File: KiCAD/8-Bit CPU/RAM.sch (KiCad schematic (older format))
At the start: 10 parts, among them U4 74HC1G32, U5 6264SL

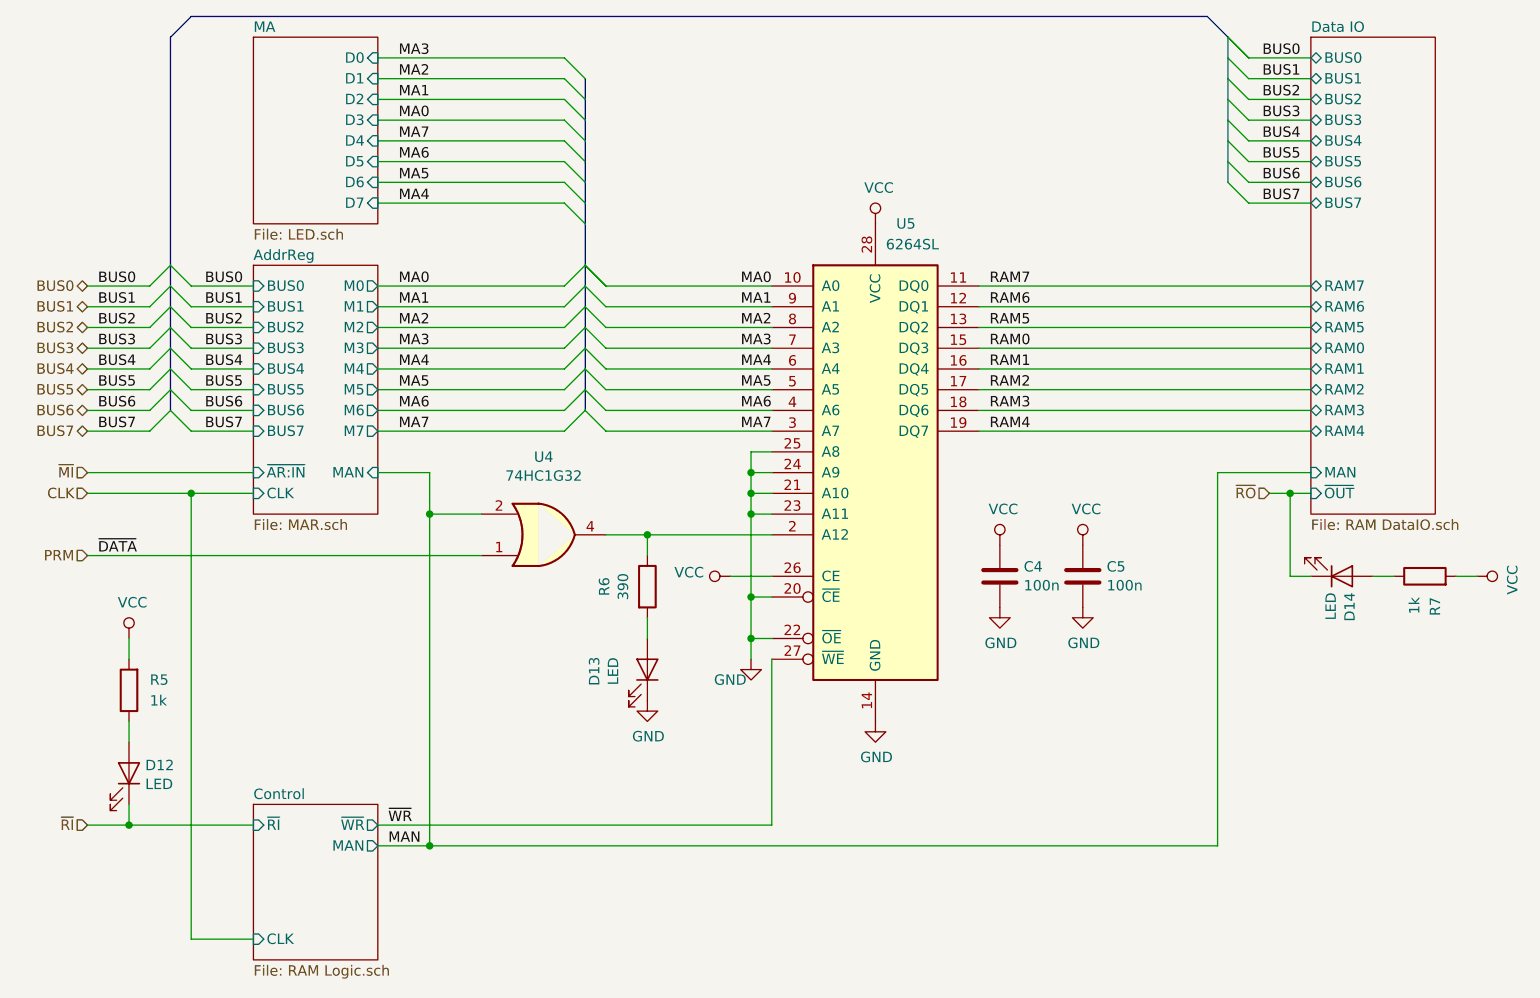
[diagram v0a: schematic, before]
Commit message: KiCAD cleanup - Revision A
Revision A Known Issues:
 * ATTiny45 has incorrect footprint
 * Flags register is redundant (The ATMega16's output port is a register)
 * Power jack pinout is wrong (12V shorted to ground)
 * Step counter reset logic is wrong (Active high signalling, Active low input)
 * ALU output indicator not connected
 * HLT indicator missing
 * EEPROMs can't be page written due to addressing setup (minor annoyance)
 * Flags Logic uses NAND gates instead of AND (fixed on the board I built)
 * Programmer needs to be able to toggle EEPROM outputs and Addressing Devices
    with different signals to enable reading.
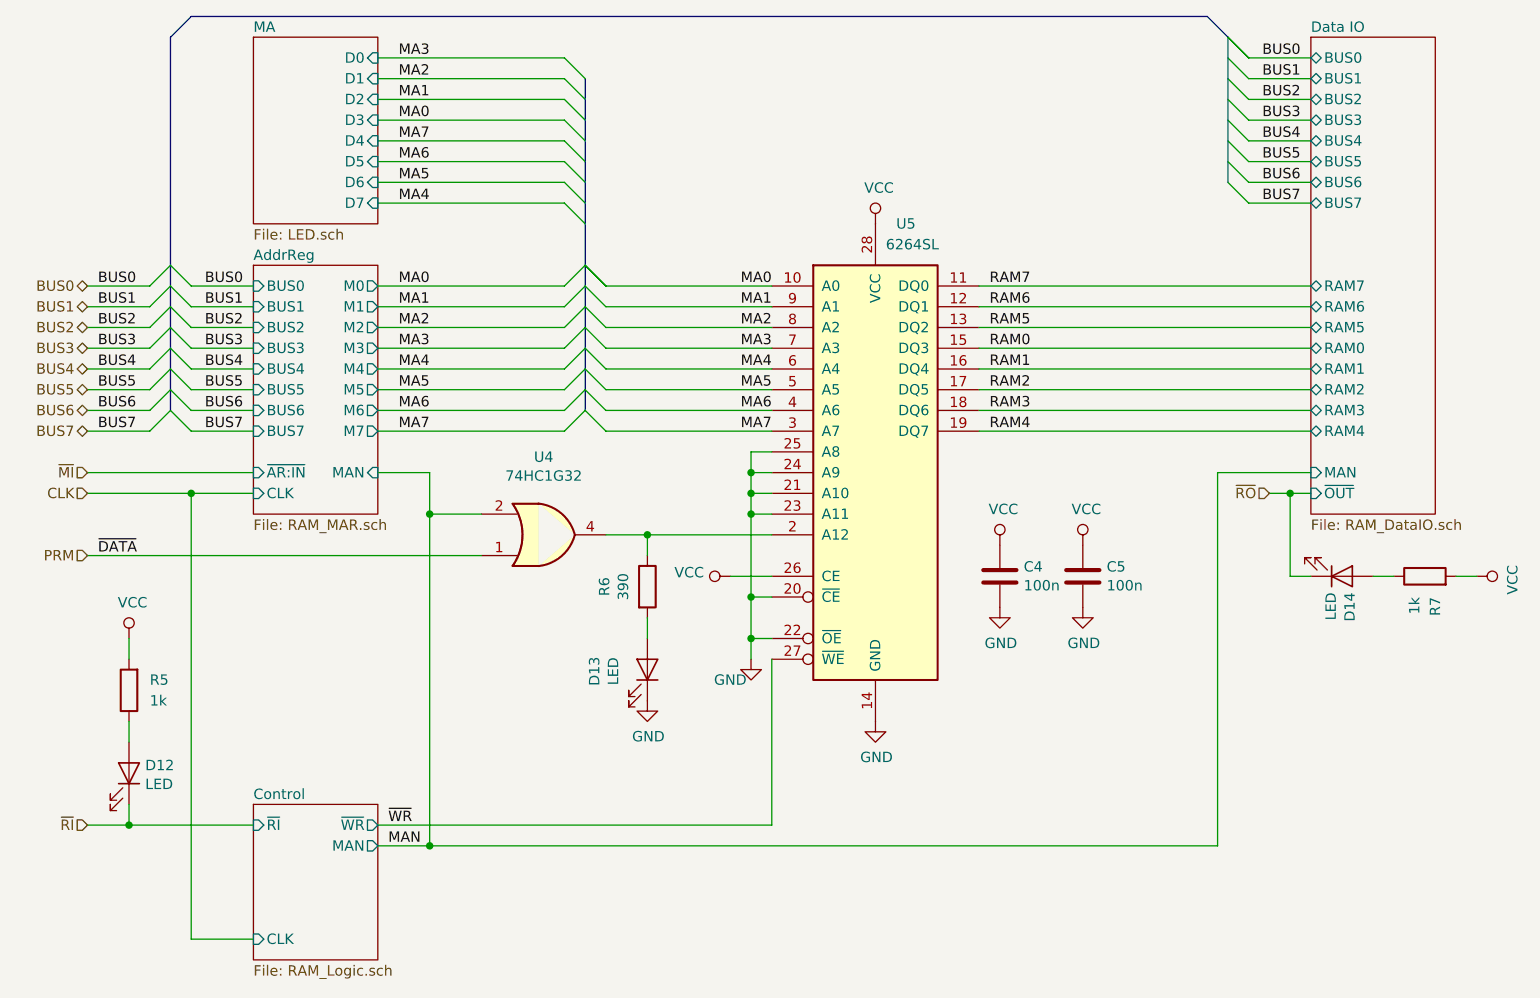
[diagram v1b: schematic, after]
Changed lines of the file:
@@
 $Descr A4 11693 8268
 encoding utf-8
-Sheet 4 30
+Sheet 4 29
 Title ""
 Date ""
@@
 U 5D5738D6
 F0 "AddrReg" 50
-F1 "MAR.sch" 50
+F1 "RAM_MAR.sch" 50
 F2 "M0" O R 3800 2600 50
 F3 "M2" O R 3800 2800 50
@@
 U 5D450B31
 F0 "Data IO" 50
-F1 "RAM DataIO.sch" 50
+F1 "RAM_DataIO.sch" 50
 F2 "RAM0" B L 8300 2900 50
 F3 "RAM1" B L 8300 3000 50
@@
 U 5D4645A0
 F0 "Control" 50
-F1 "RAM Logic.sch" 50
+F1 "RAM_Logic.sch" 50
 F2 "~RI" I L 3200 5200 50
 F3 "MAN" O R 3800 5300 50

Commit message: KiCAD files update & Gerbers
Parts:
- renumbered D14 to D12, D12 to D14, R7 to R5, R5 to R7, U5 to U4, U4 to U5
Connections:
- net GND: no longer D13.1 (K)
- net VCC: now also D13.2 (A)
- net at R6.2: now also D13.1 (K); no longer D13.2 (A)
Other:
- moved on the sheet: D13
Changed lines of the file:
@@
 Title ""
 Date ""
-Rev ""
+Rev "C"
 Comp ""
 Comment1 ""
@@
 $EndDescr
 $Comp
-L power:GND #PWR023
+L power:GND #PWR028
 U 1 1 5D6B09A3
 P 5600 4400
-F 0 "#PWR023" H 5600 4150 50  0001 C CNN
+F 0 "#PWR028" H 5600 4150 50  0001 C CNN
 F 1 "GND" H 5500 4300 50  0000 C CNN
 F 2 "" H 5600 4400 50  0001 C CNN
@@
 	5600 3700 5600 3600
 $Comp
-L power:GND #PWR025
+L power:GND #PWR029
 U 1 1 5D6B12D2
 P 6200 4700
-F 0 "#PWR025" H 6200 4450 50  0001 C CNN
+F 0 "#PWR029" H 6200 4450 50  0001 C CNN
 F 1 "GND" H 6205 4527 50  0000 C CNN
 F 2 "" H 6200 4700 50  0001 C CNN
@@
 $EndComp
 $Comp
-L power:VCC #PWR024
+L power:VCC #PWR020
 U 1 1 5D6B14C7
 P 6200 2300
-F 0 "#PWR024" H 6200 2150 50  0001 C CNN
+F 0 "#PWR020" H 6200 2150 50  0001 C CNN
 F 1 "VCC" H 6217 2473 50  0000 C CNN
 F 2 "" H 6200 2300 50  0001 C CNN
@@
 RAM0
 $Comp
-L power:VCC #PWR022
+L power:VCC #PWR023
 U 1 1 5D6B2F53
 P 5500 4000
-F 0 "#PWR022" H 5500 3850 50  0001 C CNN
+F 0 "#PWR023" H 5500 3850 50  0001 C CNN
 F 1 "VCC" V 5518 4127 50  0000 L CNN
 F 2 "" H 5500 4000 50  0001 C CNN
@@
 AR Path="/5D5738D6/5D6B415D" Ref="#PWR?"  Part="1"
 AR Path="/5D6B415D" Ref="#PWR?"  Part="1"
-AR Path="/5D643828/5D6B415D" Ref="#PWR026"  Part="1"
-F 0 "#PWR026" H 6800 3700 50  0001 C CNN
+AR Path="/5D643828/5D6B415D" Ref="#PWR021"  Part="1"
+F 0 "#PWR021" H 6800 3700 50  0001 C CNN
 F 1 "VCC" H 6817 4023 50  0000 C CNN
 F 2 "" H 6800 3850 50  0001 C CNN
@@
 AR Path="/5D5738D6/5D6B4163" Ref="#PWR?"  Part="1"
 AR Path="/5D6B4163" Ref="#PWR?"  Part="1"
-AR Path="/5D643828/5D6B4163" Ref="#PWR027"  Part="1"
-F 0 "#PWR027" H 6800 3900 50  0001 C CNN
+AR Path="/5D643828/5D6B4163" Ref="#PWR025"  Part="1"
+F 0 "#PWR025" H 6800 3900 50  0001 C CNN
 F 1 "GND" H 6805 3977 50  0000 C CNN
 F 2 "" H 6800 4150 50  0001 C CNN
@@
 	1    0    0    -1
 $EndComp
-$Comp
-L Device:LED D?
-U 1 1 5D48A9C1
-P 5100 4450
-AR Path="/5D3DC7AE/5D48A9C1" Ref="D?"  Part="1"
-AR Path="/5D3D71F3/5D48A9C1" Ref="D?"  Part="1"
-AR Path="/5D5298D8/5D48A9C1" Ref="D?"  Part="1"
-AR Path="/5D3D7710/5D48A9C1" Ref="D?"  Part="1"
-AR Path="/5D3D942F/5D48A9C1" Ref="D?"  Part="1"
-AR Path="/5D3C9EC3/5D3E8F83/5D48A9C1" Ref="D?"  Part="1"
-AR Path="/5D3C9EC3/5D3EDA47/5D48A9C1" Ref="D?"  Part="1"
-AR Path="/5D3C9EC3/5D3DA7A8/5D48A9C1" Ref="D?"  Part="1"
-AR Path="/5D3ECF82/5D3C9EC3/5D3EDA47/5D48A9C1" Ref="D?"  Part="1"
-AR Path="/5D3ECF82/5D3D7710/5D48A9C1" Ref="D?"  Part="1"
-AR Path="/5D3EFC6E/5D3EDA47/5D48A9C1" Ref="D?"  Part="1"
-AR Path="/5D3EFC78/5D48A9C1" Ref="D?"  Part="1"
-AR Path="/5D3EFC6E/5D4A89E7/5D48A9C1" Ref="D?"  Part="1"
-AR Path="/5D436CA5/5D48A9C1" Ref="D?"  Part="1"
-AR Path="/5D6F649D/5D48A9C1" Ref="D?"  Part="1"
-AR Path="/5D430931/5D48A9C1" Ref="D?"  Part="1"
-AR Path="/5D450B31/5D5FFFE8/5D48A9C1" Ref="D?"  Part="1"
-AR Path="/5D48A9C1" Ref="D?"  Part="1"
-AR Path="/5D643828/5D48A9C1" Ref="D13"  Part="1"
-F 0 "D13" H 5092 4195 50  0000 C CNN
-F 1 "LED" H 5092 4286 50  0000 C CNN
-F 2 "LED_SMD:LED_0805_2012Metric" H 5100 4450 50  0001 C CNN
-F 3 "~" H 5100 4450 50  0001 C CNN
-	1    5100 4450
-	0    1    -1   0
-$EndComp
 Wire Wire Line
 	5100 4200 5100 4300
-$Comp
-L power:GND #PWR021
-U 1 1 5D494D9B
-P 5100 4600
-F 0 "#PWR021" H 5100 4350 50  0001 C CNN
-F 1 "GND" H 5105 4427 50  0000 C CNN
-F 2 "" H 5100 4600 50  0001 C CNN
-F 3 "" H 5100 4600 50  0001 C CNN
-	1    5100 4600
-	1    0    0    -1
-$EndComp
 Wire Wire Line
 	4050 3500 4050 3700
@@
 	5100 3800 5700 3800
 $Comp
-L jcf-digital:74HC1G32 U4
+L jcf-digital:74HC1G32 U5
 U 1 1 5D5F286E
 P 4600 3800
-F 0 "U4" H 4600 3425 50  0000 C CNN
+F 0 "U5" H 4600 3425 50  0000 C CNN
 F 1 "74HC1G32" H 4600 3516 50  0000 C CNN
 F 2 "Package_SO:TSOP-5_1.65x3.05mm_P0.95mm" H 4600 3800 50  0001 C CNN
@@
 AR Path="/5D5738D6/5D601AB0" Ref="#PWR?"  Part="1"
 AR Path="/5D601AB0" Ref="#PWR?"  Part="1"
-AR Path="/5D643828/5D601AB0" Ref="#PWR028"  Part="1"
-F 0 "#PWR028" H 7200 3700 50  0001 C CNN
+AR Path="/5D643828/5D601AB0" Ref="#PWR022"  Part="1"
+F 0 "#PWR022" H 7200 3700 50  0001 C CNN
 F 1 "VCC" H 7217 4023 50  0000 C CNN
 F 2 "" H 7200 3850 50  0001 C CNN
@@
 AR Path="/5D5738D6/5D601AB6" Ref="#PWR?"  Part="1"
 AR Path="/5D601AB6" Ref="#PWR?"  Part="1"
-AR Path="/5D643828/5D601AB6" Ref="#PWR029"  Part="1"
-F 0 "#PWR029" H 7200 3900 50  0001 C CNN
+AR Path="/5D643828/5D601AB6" Ref="#PWR026"  Part="1"
+F 0 "#PWR026" H 7200 3900 50  0001 C CNN
 F 1 "GND" H 7205 3977 50  0000 C CNN
 F 2 "" H 7200 4150 50  0001 C CNN
@@
 ~DATA
 $Comp
-L jcf-digital:6264SL U5
+L jcf-digital:6264SL U4
 U 1 1 5D651472
 P 6200 3400
-F 0 "U5" H 6300 4500 50  0000 L CNN
+F 0 "U4" H 6300 4500 50  0000 L CNN
 F 1 "6264SL" H 6250 4400 50  0000 L CNN
 F 2 "jcf:SOIC-28W-LY6264" H 6200 3600 50  0001 C CNN
@@
 AR Path="/5D5A6551/5D5E9319" Ref="R?"  Part="1"
 AR Path="/5D6D875D/5D523C20/5D5E9319" Ref="R?"  Part="1"
-AR Path="/5D643828/5D5E9319" Ref="R5"  Part="1"
-F 0 "R5" H 2500 4500 50  0000 R CNN
+AR Path="/5D643828/5D5E9319" Ref="R7"  Part="1"
+F 0 "R7" H 2500 4500 50  0000 R CNN
 F 1 "1k" H 2500 4600 50  0000 R CNN
 F 2 "Resistor_SMD:R_0805_2012Metric" V 2530 4550 50  0001 C CNN
@@
 AR Path="/5D523C20/5D5E931F" Ref="D?"  Part="1"
 AR Path="/5D6D875D/5D523C20/5D5E931F" Ref="D?"  Part="1"
-AR Path="/5D643828/5D5E931F" Ref="D12"  Part="1"
-F 0 "D12" V 2638 5028 50  0000 L CNN
+AR Path="/5D643828/5D5E931F" Ref="D14"  Part="1"
+F 0 "D14" V 2638 5028 50  0000 L CNN
 F 1 "LED" V 2547 5028 50  0000 L CNN
 F 2 "LED_SMD:LED_0805_2012Metric" H 2600 4950 50  0001 C CNN
@@
 	2600 5200 3200 5200
 $Comp
-L power:VCC #PWR020
+L power:VCC #PWR027
 U 1 1 5D5ED2EF
 P 2600 4300
-F 0 "#PWR020" H 2600 4150 50  0001 C CNN
+F 0 "#PWR027" H 2600 4150 50  0001 C CNN
 F 1 "VCC" H 2617 4473 50  0000 C CNN
 F 2 "" H 2600 4300 50  0001 C CNN
@@
 	8200 3600 8300 3600
 $Comp
-L power:VCC #PWR030
+L power:VCC #PWR024
 U 1 1 5D5F0DA9
 P 9100 4000
-F 0 "#PWR030" H 9100 3850 50  0001 C CNN
+F 0 "#PWR024" H 9100 3850 50  0001 C CNN
 F 1 "VCC" H 9117 4173 50  0000 C CNN
 F 2 "" H 9100 4000 50  0001 C CNN
@@
 AR Path="/5D523C20/5D5F0DA0" Ref="D?"  Part="1"
 AR Path="/5D6D875D/5D523C20/5D5F0DA0" Ref="D?"  Part="1"
-AR Path="/5D643828/5D5F0DA0" Ref="D14"  Part="1"
-F 0 "D14" V 8488 4078 50  0000 L CNN
+AR Path="/5D643828/5D5F0DA0" Ref="D12"  Part="1"
+F 0 "D12" V 8488 4078 50  0000 L CNN
 F 1 "LED" V 8397 4078 50  0000 L CNN
 F 2 "LED_SMD:LED_0805_2012Metric" H 8450 4000 50  0001 C CNN
@@
 AR Path="/5D5A6551/5D5F0D9A" Ref="R?"  Part="1"
 AR Path="/5D6D875D/5D523C20/5D5F0D9A" Ref="R?"  Part="1"
-AR Path="/5D643828/5D5F0D9A" Ref="R7"  Part="1"
-F 0 "R7" H 8750 3950 50  0000 R CNN
+AR Path="/5D643828/5D5F0D9A" Ref="R5"  Part="1"
+F 0 "R5" H 8750 3950 50  0000 R CNN
 F 1 "1k" H 8750 4050 50  0000 R CNN
 F 2 "Resistor_SMD:R_0805_2012Metric" V 8780 4000 50  0001 C CNN
@@
 	0    -1   -1   0
 $EndComp
+$Comp
+L Device:LED D?
+U 1 1 5D48A9C1
+P 5100 4450
+AR Path="/5D3DC7AE/5D48A9C1" Ref="D?"  Part="1"
+AR Path="/5D3D71F3/5D48A9C1" Ref="D?"  Part="1"
+AR Path="/5D5298D8/5D48A9C1" Ref="D?"  Part="1"
+AR Path="/5D3D7710/5D48A9C1" Ref="D?"  Part="1"
+AR Path="/5D3D942F/5D48A9C1" Ref="D?"  Part="1"
+AR Path="/5D3C9EC3/5D3E8F83/5D48A9C1" Ref="D?"  Part="1"
+AR Path="/5D3C9EC3/5D3EDA47/5D48A9C1" Ref="D?"  Part="1"
+AR Path="/5D3C9EC3/5D3DA7A8/5D48A9C1" Ref="D?"  Part="1"
+AR Path="/5D3ECF82/5D3C9EC3/5D3EDA47/5D48A9C1" Ref="D?"  Part="1"
+AR Path="/5D3ECF82/5D3D7710/5D48A9C1" Ref="D?"  Part="1"
+AR Path="/5D3EFC6E/5D3EDA47/5D48A9C1" Ref="D?"  Part="1"
+AR Path="/5D3EFC78/5D48A9C1" Ref="D?"  Part="1"
+AR Path="/5D3EFC6E/5D4A89E7/5D48A9C1" Ref="D?"  Part="1"
+AR Path="/5D436CA5/5D48A9C1" Ref="D?"  Part="1"
+AR Path="/5D6F649D/5D48A9C1" Ref="D?"  Part="1"
+AR Path="/5D430931/5D48A9C1" Ref="D?"  Part="1"
+AR Path="/5D450B31/5D5FFFE8/5D48A9C1" Ref="D?"  Part="1"
+AR Path="/5D48A9C1" Ref="D?"  Part="1"
+AR Path="/5D643828/5D48A9C1" Ref="D13"  Part="1"
+F 0 "D13" H 5092 4195 50  0000 C CNN
+F 1 "LED" H 5092 4286 50  0000 C CNN
+F 2 "LED_SMD:LED_0805_2012Metric" H 5100 4450 50  0001 C CNN
+F 3 "~" H 5100 4450 50  0001 C CNN
+	1    5100 4450
+	0    -1   1    0
+$EndComp
+$Comp
+L power:VCC #PWR030
+U 1 1 5D7413F3
+P 5000 4750
+F 0 "#PWR030" H 5000 4600 50  0001 C CNN
+F 1 "VCC" V 5018 4877 50  0000 L CNN
+F 2 "" H 5000 4750 50  0001 C CNN
+F 3 "" H 5000 4750 50  0001 C CNN
+	1    5000 4750
+	0    -1   -1   0
+$EndComp
+Wire Wire Line
+	5000 4750 5100 4750
+Wire Wire Line
+	5100 4750 5100 4600
 Wire Bus Line
 	7900 1400 7900 2100
